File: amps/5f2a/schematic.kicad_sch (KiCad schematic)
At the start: 31 parts, among them T2 SE 5k:8

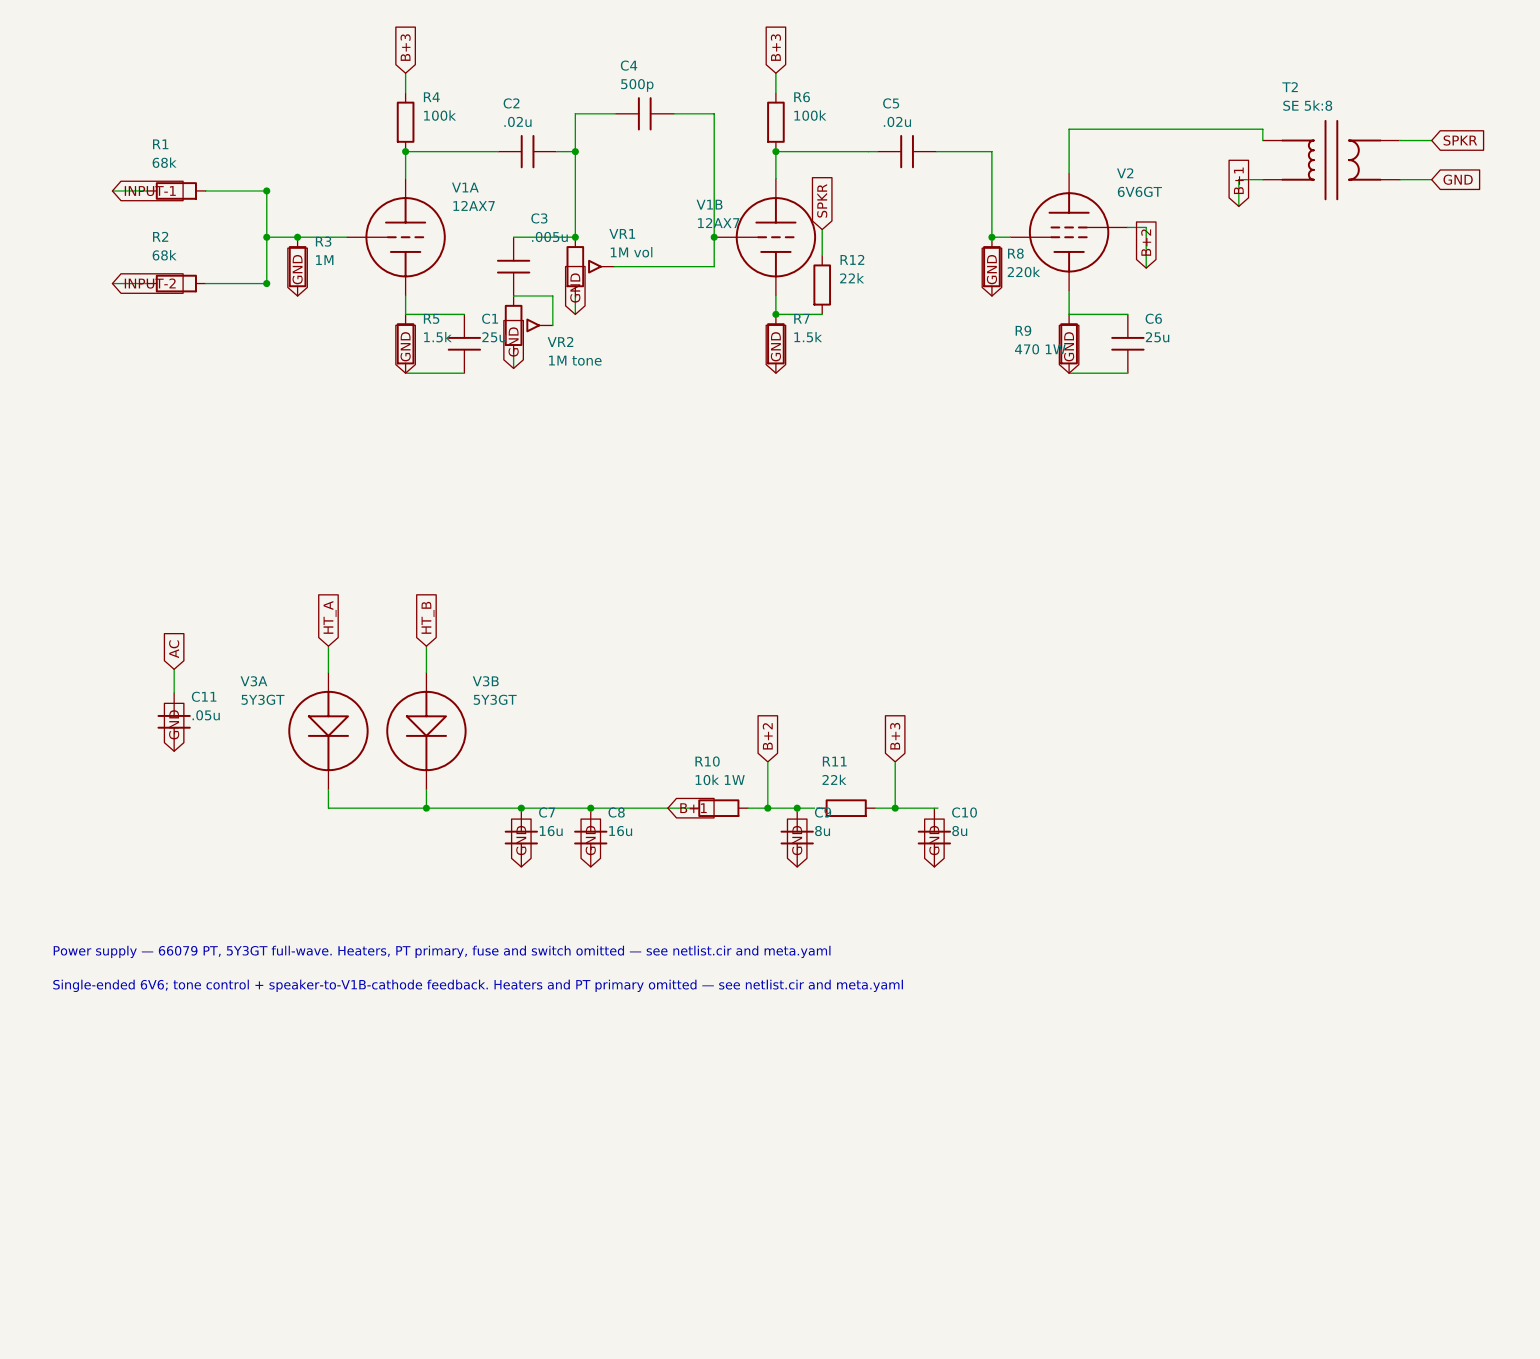
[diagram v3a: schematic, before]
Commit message: Fix: rotated global labels lettered their net names outside the flag
Every global label this pipeline emitted carried (justify left) regardless of
rotation. KiCanvas — like KiCad — draws label text horizontally at 0/180 and
vertically at 90/270 and reads WHICH SIDE of the anchor it letters on from the
justification, so at 180 and 270 the name printed outside an empty flag
outline, struck through by the very wire it names: 219 labels at 180 deg
(including the input-jack flags at top-left of nearly every sheet, the first
glyphs a visitor reads) and 792 GND/rail flags at 270 whose names squeezed at
the flag mouth instead of lettering down the body. The library already
compensated rotation for property text (`pa`); this mirrors that logic for
global labels: justify right at 180/270, left at 0/90.

check_schematics gains the geometry clause whose absence let all 1011
instances through a "no lettering through circuitry" pass: it modelled the
flag box but never the label TEXT, so a name rendered on the wrong side was
invisible to it. The gate now proves justification compensates rotation on
every global label.

Two more things this exposed, fixed in the same engine pass:

- Placement now measures with the renderer's own Newstroke advance table
  (extracted from the vendored kicanvas.js) instead of a flat 0.68-em prose
  average that under-read part lettering by a quarter — the mechanism behind
  every "metered clean, printed through its neighbour" incident. The GATE
  deliberately keeps the coarse ruler: re-ruling it with renderer truth was
  tried and red-flagged 28 of 34 sheets over abutments three visual passes
  had already judged sub-visual (the two-rulers note in schematic_lib.py).
- place_captions' escape ladder runs further, because a banner caption
  measured truly is half again wider than the old estimate believed.

All 34 schematics regenerated; full gate suite green.

🤖 Generated with [Claude Code](https://claude.com/claude-code)

Co-Authored-By: Claude Fable 5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
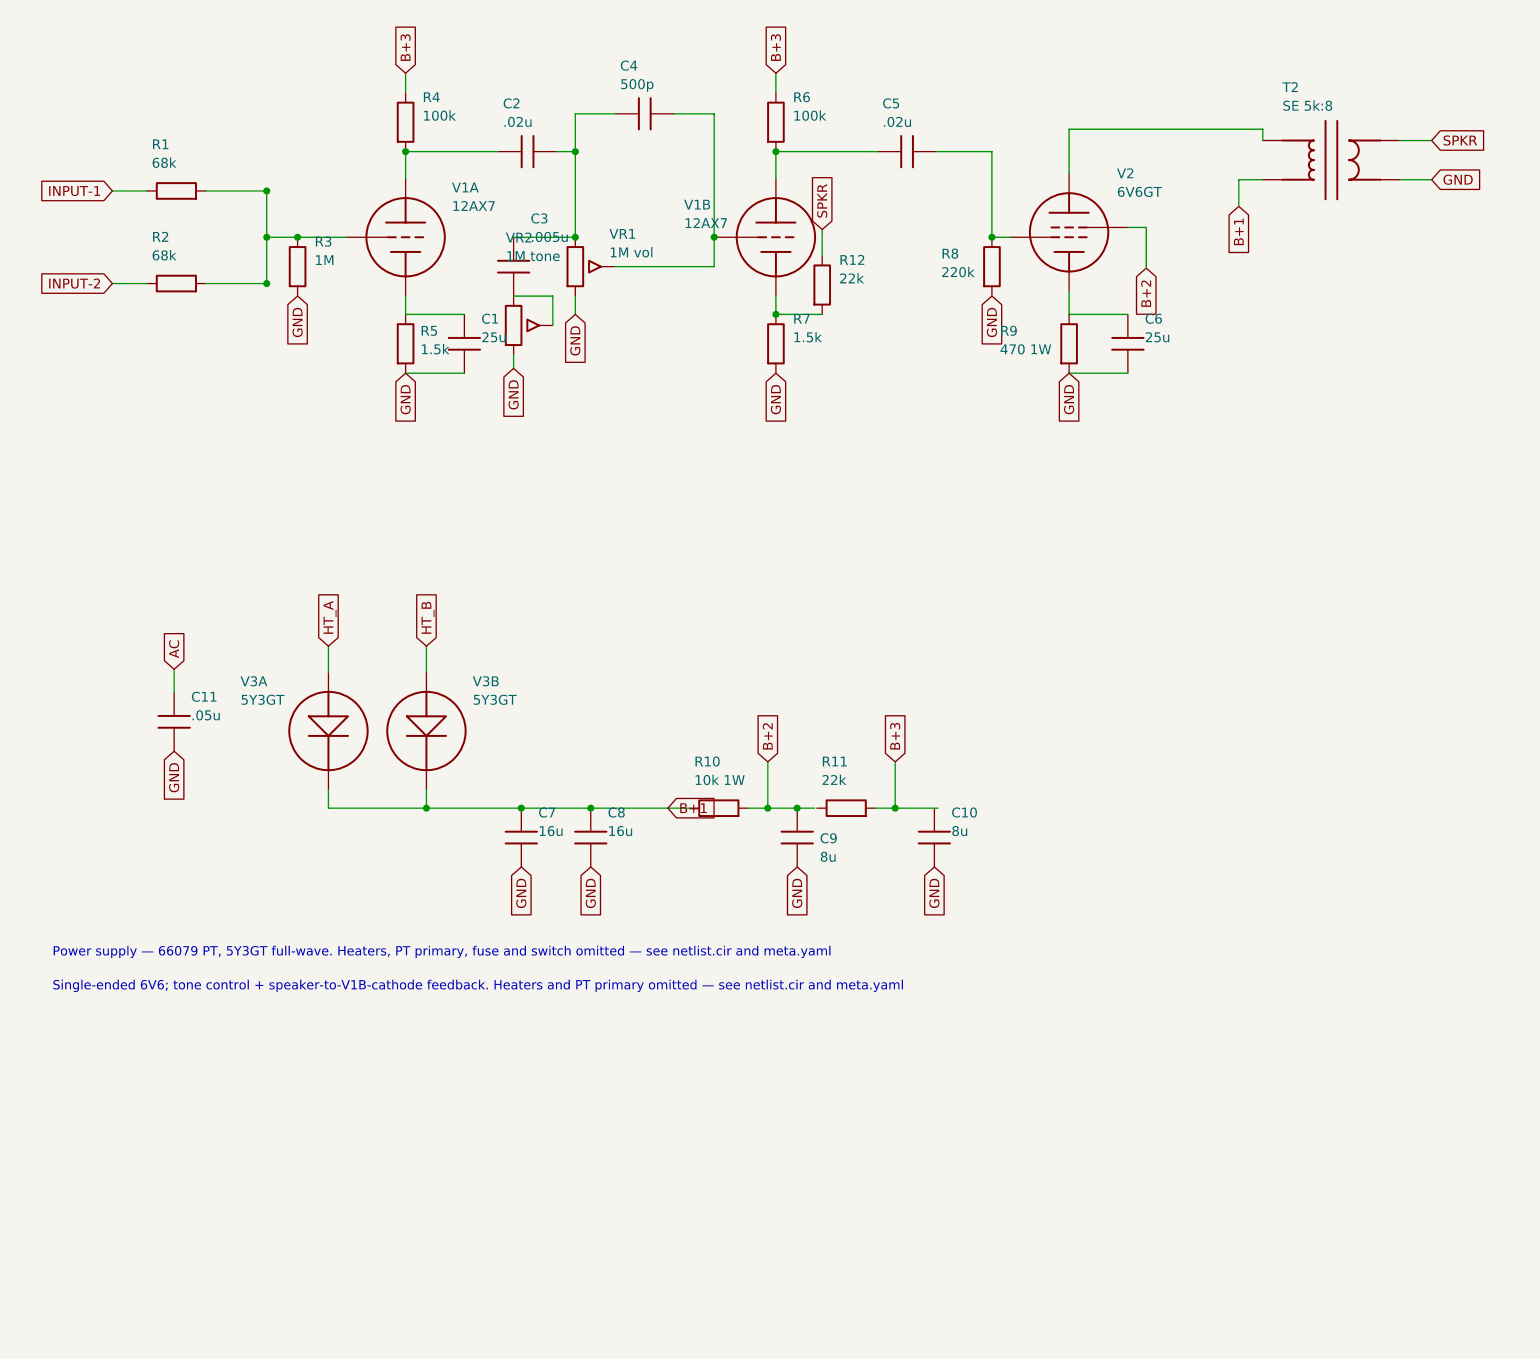
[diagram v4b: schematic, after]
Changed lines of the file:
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@@
     (comment 3 "Values read from: https://el34world.com/charts/Schematics/files/Fender/Fender_princeton_5f2a.pdf"))
   (global_label "INPUT-1" (shape input) (at 20.4724 32.278 180)
-    (effects (font (size 1.27 1.27)) (justify left)))
+    (effects (font (size 1.27 1.27)) (justify right)))
   (wire (pts (xy 20.4724 32.278) (xy 24.9524 32.278))
     (stroke (width 0) (type default)))
@@
     (stroke (width 0) (type default)))
   (global_label "INPUT-2" (shape input) (at 20.4724 44.278 180)
-    (effects (font (size 1.27 1.27)) (justify left)))
+    (effects (font (size 1.27 1.27)) (justify right)))
   (wire (pts (xy 20.4724 44.278) (xy 24.9524 44.278))
     (stroke (width 0) (type default)))
@@
     (property "Value" "1M" (at 46.6724 41.288 0) (effects (font (size 1.27 1.27)) (justify left))))
   (global_label "GND" (shape input) (at 44.4724 45.898 270)
-    (effects (font (size 1.27 1.27)) (justify left)))
+    (effects (font (size 1.27 1.27)) (justify right)))
   (symbol (lib_id "cx:TRIODE") (at 58.4724 38.278 0) (unit 1)
     (in_bom yes) (on_board yes)
@@
   (symbol (lib_id "cx:R") (at 58.4724 52.088 0) (unit 1)
     (in_bom yes) (on_board yes)
-    (property "Reference" "R5" (at 60.6724 48.888 0) (effects (font (size 1.27 1.27)) (justify left)))
-    (property "Value" "1.5k" (at 60.6724 51.288 0) (effects (font (size 1.27 1.27)) (justify left))))
+    (property "Reference" "R5" (at 60.3884 50.448 0) (effects (font (size 1.27 1.27)) (justify left)))
+    (property "Value" "1.5k" (at 60.3884 52.848 0) (effects (font (size 1.27 1.27)) (justify left))))
   (symbol (lib_id "cx:C") (at 66.0924 52.088 0) (unit 1)
     (in_bom yes) (on_board yes)
@@
     (stroke (width 0) (type default)))
   (global_label "GND" (shape input) (at 58.4724 55.898 270)
-    (effects (font (size 1.27 1.27)) (justify left)))
+    (effects (font (size 1.27 1.27)) (justify right)))
   (wire (pts (xy 58.4724 30.658) (xy 58.4724 27.178))
     (stroke (width 0) (type default)))
@@
     (stroke (width 0) (type default)))
   (global_label "GND" (shape input) (at 80.4724 48.278 270)
-    (effects (font (size 1.27 1.27)) (justify left)))
+    (effects (font (size 1.27 1.27)) (justify right)))
   (wire (pts (xy 85.5524 42.088) (xy 98.4724 42.088))
     (stroke (width 0) (type default)))
@@
   (symbol (lib_id "cx:POT") (at 72.4724 49.708 0) (unit 1)
     (in_bom yes) (on_board yes)
-    (property "Reference" "VR2" (at 76.8724 51.908 0) (effects (font (size 1.27 1.27)) (justify left)))
-    (property "Value" "1M tone" (at 76.8724 54.308 0) (effects (font (size 1.27 1.27)) (justify left))))
+    (property "Reference" "VR2" (at 71.4564 38.368 0) (effects (font (size 1.27 1.27)) (justify left)))
+    (property "Value" "1M tone" (at 71.4564 40.768 0) (effects (font (size 1.27 1.27)) (justify left))))
   (wire (pts (xy 77.5524 49.708) (xy 77.5524 45.898))
     (stroke (width 0) (type default)))
@@
     (stroke (width 0) (type default)))
   (global_label "GND" (shape input) (at 72.4724 55.278 270)
-    (effects (font (size 1.27 1.27)) (justify left)))
+    (effects (font (size 1.27 1.27)) (justify right)))
   (symbol (lib_id "cx:TRIODE") (at 106.472 38.278 0) (unit 1)
     (in_bom yes) (on_board yes)
-    (property "Reference" "V1B" (at 96.1744 34.098 0) (effects (font (size 1.27 1.27)) (justify left)))
-    (property "Value" "12AX7" (at 96.1744 36.498 0) (effects (font (size 1.27 1.27)) (justify left))))
+    (property "Reference" "V1B" (at 94.5678 34.098 0) (effects (font (size 1.27 1.27)) (justify left)))
+    (property "Value" "12AX7" (at 94.5678 36.498 0) (effects (font (size 1.27 1.27)) (justify left))))
   (wire (pts (xy 98.4724 38.278) (xy 98.8524 38.278))
     (stroke (width 0) (type default)))
@@
     (property "Value" "1.5k" (at 108.672 51.288 0) (effects (font (size 1.27 1.27)) (justify left))))
   (global_label "GND" (shape input) (at 106.472 55.898 270)
-    (effects (font (size 1.27 1.27)) (justify left)))
+    (effects (font (size 1.27 1.27)) (justify right)))
   (wire (pts (xy 106.472 48.278) (xy 112.472 48.278))
     (stroke (width 0) (type default)))
@@
   (symbol (lib_id "cx:R") (at 134.472 42.088 0) (unit 1)
     (in_bom yes) (on_board yes)
-    (property "Reference" "R8" (at 136.388 40.448 0) (effects (font (size 1.27 1.27)) (justify left)))
-    (property "Value" "220k" (at 136.388 42.848 0) (effects (font (size 1.27 1.27)) (justify left))))
+    (property "Reference" "R8" (at 127.901 40.448 0) (effects (font (size 1.27 1.27)) (justify left)))
+    (property "Value" "220k" (at 127.901 42.848 0) (effects (font (size 1.27 1.27)) (justify left))))
   (global_label "GND" (shape input) (at 134.472 45.898 270)
-    (effects (font (size 1.27 1.27)) (justify left)))
+    (effects (font (size 1.27 1.27)) (justify right)))
   (wire (pts (xy 144.472 45.263) (xy 144.472 48.278))
     (stroke (width 0) (type default)))
   (symbol (lib_id "cx:R") (at 144.472 52.088 0) (unit 1)
     (in_bom yes) (on_board yes)
-    (property "Reference" "R9" (at 137.375 50.448 0) (effects (font (size 1.27 1.27)) (justify left)))
-    (property "Value" "470 1W" (at 137.375 52.848 0) (effects (font (size 1.27 1.27)) (justify left))))
+    (property "Reference" "R9" (at 135.507 50.448 0) (effects (font (size 1.27 1.27)) (justify left)))
+    (property "Value" "470 1W" (at 135.507 52.848 0) (effects (font (size 1.27 1.27)) (justify left))))
   (symbol (lib_id "cx:C") (at 152.092 52.088 0) (unit 1)
     (in_bom yes) (on_board yes)
@@
     (stroke (width 0) (type default)))
   (global_label "GND" (shape input) (at 144.472 55.898 270)
-    (effects (font (size 1.27 1.27)) (justify left)))
+    (effects (font (size 1.27 1.27)) (justify right)))
   (wire (pts (xy 152.092 37.008) (xy 154.472 37.008))
     (stroke (width 0) (type default)))
@@
     (stroke (width 0) (type default)))
   (global_label "B+2" (shape input) (at 154.472 42.278 270)
-    (effects (font (size 1.27 1.27)) (justify left)))
+    (effects (font (size 1.27 1.27)) (justify right)))
   (wire (pts (xy 144.472 30.023) (xy 144.472 24.278))
     (stroke (width 0) (type default)))
@@
     (stroke (width 0) (type default)))
   (global_label "B+1" (shape input) (at 166.472 34.278 270)
-    (effects (font (size 1.27 1.27)) (justify left)))
+    (effects (font (size 1.27 1.27)) (justify right)))
   (wire (pts (xy 187.362 25.738) (xy 191.472 25.738))
     (stroke (width 0) (type default)))
@@
     (property "Value" ".05u" (at 30.6724 100.288 0) (effects (font (size 1.27 1.27)) (justify left))))
   (global_label "GND" (shape input) (at 28.4724 104.898 270)
-    (effects (font (size 1.27 1.27)) (justify left)))
+    (effects (font (size 1.27 1.27)) (justify right)))
   (global_label "HT_A" (shape input) (at 48.4724 91.278 90)
     (effects (font (size 1.27 1.27)) (justify left)))
@@
     (property "Value" "16u" (at 75.6724 115.288 0) (effects (font (size 1.27 1.27)) (justify left))))
   (global_label "GND" (shape input) (at 73.4724 119.898 270)
-    (effects (font (size 1.27 1.27)) (justify left)))
+    (effects (font (size 1.27 1.27)) (justify right)))
   (junction (at 82.4724 112.278) (diameter 0) (color 0 0 0 0))
   (symbol (lib_id "cx:C") (at 82.4724 116.088 0) (unit 1)
@@
     (property "Value" "16u" (at 84.6724 115.288 0) (effects (font (size 1.27 1.27)) (justify left))))
   (global_label "GND" (shape input) (at 82.4724 119.898 270)
-    (effects (font (size 1.27 1.27)) (justify left)))
+    (effects (font (size 1.27 1.27)) (justify right)))
   (global_label "B+1" (shape input) (at 92.4724 112.278 0)
     (effects (font (size 1.27 1.27)) (justify left)))
@@
   (symbol (lib_id "cx:C") (at 109.232 116.088 0) (unit 1)
     (in_bom yes) (on_board yes)
-    (property "Reference" "C9" (at 111.432 112.888 0) (effects (font (size 1.27 1.27)) (justify left)))
-    (property "Value" "8u" (at 111.432 115.288 0) (effects (font (size 1.27 1.27)) (justify left))))
+    (property "Reference" "C9" (at 112.164 116.226 0) (effects (font (size 1.27 1.27)) (justify left)))
+    (property "Value" "8u" (at 112.164 118.626 0) (effects (font (size 1.27 1.27)) (justify left))))
   (global_label "GND" (shape input) (at 109.232 119.898 270)
-    (effects (font (size 1.27 1.27)) (justify left)))
+    (effects (font (size 1.27 1.27)) (justify right)))
   (symbol (lib_id "cx:R") (at 115.582 112.278 90) (unit 1)
     (in_bom yes) (on_board yes)
@@
     (property "Value" "8u" (at 129.212 115.288 0) (effects (font (size 1.27 1.27)) (justify left))))
   (global_label "GND" (shape input) (at 127.012 119.898 270)
-    (effects (font (size 1.27 1.27)) (justify left)))
+    (effects (font (size 1.27 1.27)) (justify right)))
   (text "Power supply — 66079 PT, 5Y3GT full-wave. Heaters, PT primary, fuse and switch omitted — see netlist.cir and meta.yaml" (at 12.7 131.056 0)
     (effects (font (size 1.2 1.2)) (justify left)))
